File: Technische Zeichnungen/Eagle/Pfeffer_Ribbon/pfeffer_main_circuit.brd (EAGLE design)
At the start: 38 x 50 mm, 12 parts

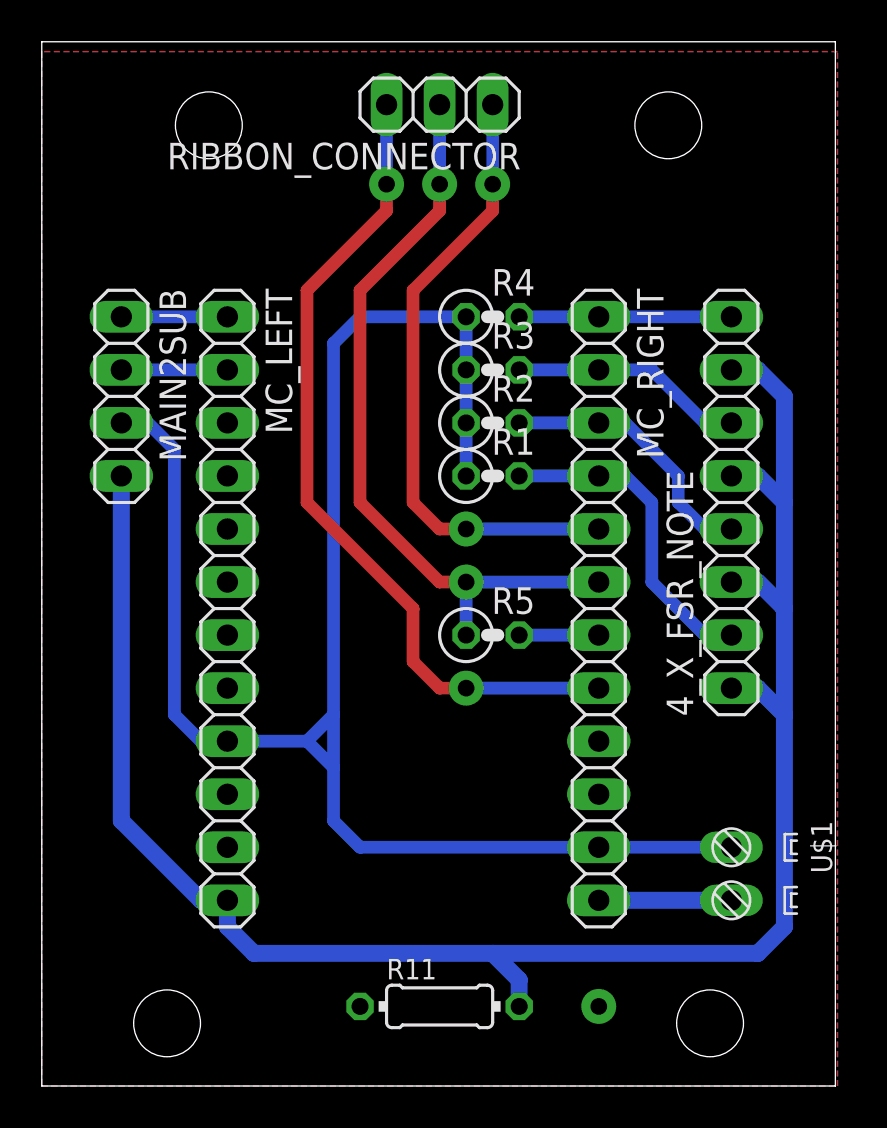
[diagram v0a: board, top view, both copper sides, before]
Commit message: added ribbon testing, firmware and applied it to the new firmware, added a new tech. drawing, added new PCB layouts
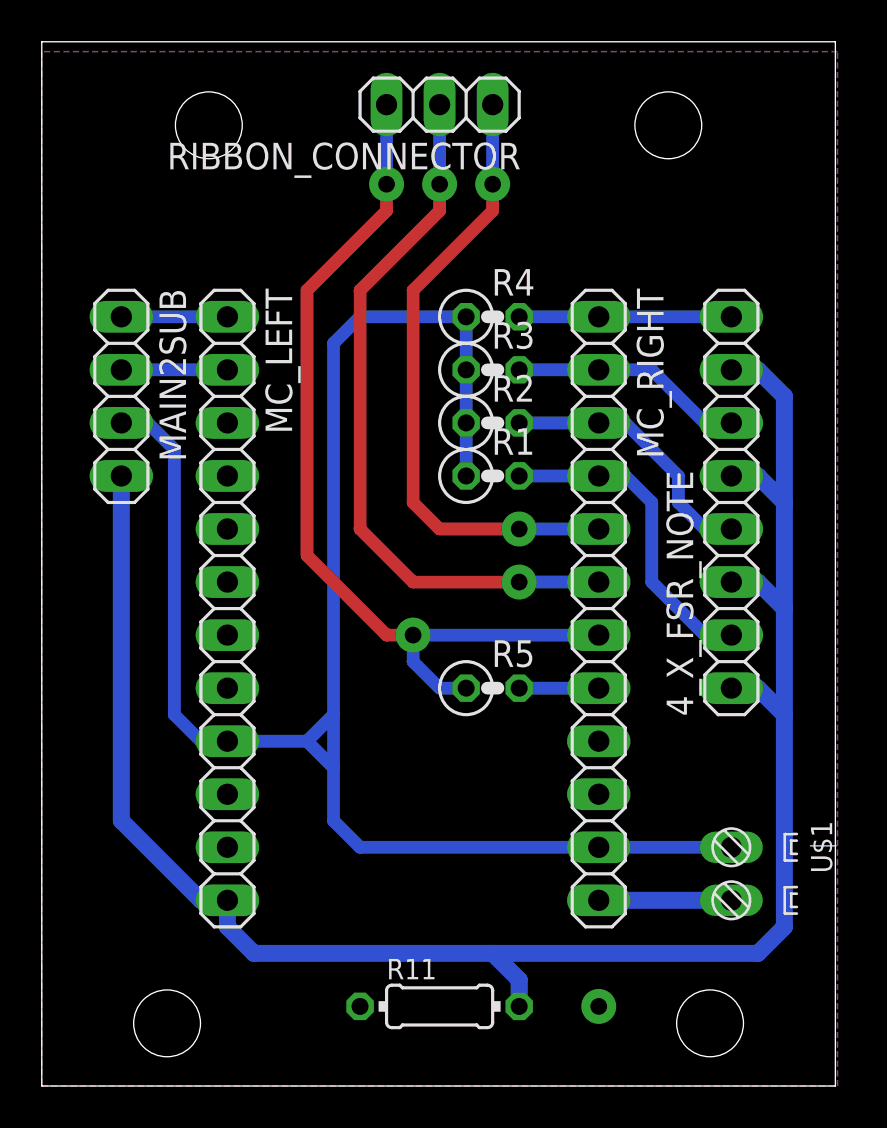
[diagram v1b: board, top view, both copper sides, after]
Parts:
- R11: value 100k -> 24
- moved R5 2.54 mm to (21.6, 19.1)
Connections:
- net N$10: now also MC_RIGHT.7, RIBBON_CONNECTOR.3; no longer MC_RIGHT.6, RIBBON_CONNECTOR.2
- net N$11: now also R5.2; no longer RIBBON_CONNECTOR.3
- net N$9: now also MC_RIGHT.6, RIBBON_CONNECTOR.2; no longer MC_RIGHT.7, R5.2
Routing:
- net N$11: track 39.8 -> 3.81 mm, vias 2 -> 0
- net N$9: track 3.81 -> 34.4 mm, vias 0 -> 2
- net N$10: track 36.2 -> 43.1 mm
- added copper zone on layer 16, net N$12
- added copper zone on layer 1, net N$13
- removed copper zone on layer 16, net GND
- removed copper zone on layer 1, net N$12
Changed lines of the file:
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@@
 <element name="R3" library="rcl" package="0207/2V" value="10k" x="21.59" y="34.29"/>
 <element name="R4" library="rcl" package="0207/2V" value="10k" x="21.59" y="36.83"/>
-<element name="R11" library="rcl" package="0204/7" value="100k" x="19.05" y="3.81"/>
+<element name="R11" library="rcl" package="0204/7" value="24" x="19.05" y="3.81"/>
 <element name="U$1" library="myDegsonConnectors" package="DS308-2.54-02P" value="DS308-02" x="33.02" y="10.16" rot="R270"/>
 <element name="RIBBON_CONNECTOR" library="pinhead" package="1X03" value="" x="19.05" y="46.99" rot="R180"/>
-<element name="R5" library="rcl" package="0207/2V" value="4.6k" x="21.59" y="21.59"/>
+<element name="R5" library="rcl" package="0207/2V" value="4.6k" x="21.59" y="19.05"/>
 </elements>
 <signals>
@@
 <wire x1="15.24" y1="11.43" x2="26.67" y2="11.43" width="0.6096" layer="16"/>
 <wire x1="13.97" y1="17.78" x2="13.97" y2="15.24" width="0.6096" layer="16"/>
-<polygon width="0.6096" layer="16">
-<vertex x="0" y="49.53"/>
-<vertex x="0" y="0"/>
-<vertex x="38.1" y="0"/>
-<vertex x="38.1" y="49.53"/>
-</polygon>
+<wire x1="26.67" y1="11.43" x2="26.67" y2="3.81" width="0" layer="19" extent="1-1"/>
+<wire x1="15.24" y1="3.81" x2="15.24" y2="11.43" width="0" layer="19" extent="16-16"/>
 </signal>
 <signal name="N$1">
@@
 <wire x1="3.81" y1="34.29" x2="8.89" y2="34.29" width="0.6096" layer="16"/>
 </signal>
+<signal name="N$5">
+<contactref element="MC_RIGHT" pad="12"/>
+<contactref element="U$1" pad="2"/>
+<wire x1="33.02" y1="8.89" x2="26.67" y2="8.89" width="0.8128" layer="16"/>
+</signal>
 <signal name="N$7">
+<contactref element="RIBBON_CONNECTOR" pad="1"/>
 <contactref element="MC_RIGHT" pad="5"/>
-<contactref element="RIBBON_CONNECTOR" pad="1"/>
-<via x="20.32" y="26.67" extent="1-16" drill="0.8" diameter="1.6764" shape="octagon"/>
+<wire x1="21.59" y1="46.99" x2="21.59" y2="43.18" width="0.6096" layer="16"/>
 <via x="21.59" y="43.18" extent="1-16" drill="0.8" diameter="1.6764" shape="octagon"/>
-<wire x1="21.59" y1="43.18" x2="21.59" y2="46.99" width="0.6096" layer="16"/>
-<wire x1="17.78" y1="38.1" x2="21.59" y2="41.91" width="0.6096" layer="1"/>
-<wire x1="21.59" y1="41.91" x2="21.59" y2="43.18" width="0.6096" layer="1"/>
-<wire x1="20.32" y1="26.67" x2="26.67" y2="26.67" width="0.6096" layer="16"/>
-<wire x1="20.32" y1="26.67" x2="19.05" y2="26.67" width="0.6096" layer="1"/>
-<wire x1="19.05" y1="26.67" x2="17.78" y2="27.94" width="0.6096" layer="1"/>
-<wire x1="17.78" y1="27.94" x2="17.78" y2="38.1" width="0.6096" layer="1"/>
+<wire x1="21.59" y1="43.18" x2="21.59" y2="41.91" width="0.6096" layer="1"/>
+<wire x1="21.59" y1="41.91" x2="17.78" y2="38.1" width="0.6096" layer="1"/>
+<via x="22.86" y="26.67" extent="1-16" drill="0.8" diameter="1.6764" shape="octagon"/>
+<wire x1="22.86" y1="26.67" x2="26.67" y2="26.67" width="0.6096" layer="16"/>
+<wire x1="17.78" y1="38.1" x2="17.78" y2="27.94" width="0.6096" layer="1"/>
+<wire x1="17.78" y1="27.94" x2="19.05" y2="26.67" width="0.6096" layer="1"/>
+<wire x1="19.05" y1="26.67" x2="22.86" y2="26.67" width="0.6096" layer="1"/>
 </signal>
-<signal name="N$10">
+<signal name="N$9">
 <contactref element="RIBBON_CONNECTOR" pad="2"/>
 <contactref element="MC_RIGHT" pad="6"/>
@@
 <via x="19.05" y="43.18" extent="1-16" drill="0.8" diameter="1.6764" shape="octagon"/>
 <wire x1="19.05" y1="43.18" x2="19.05" y2="41.91" width="0.6096" layer="1"/>
-<wire x1="15.24" y1="38.1" x2="19.05" y2="41.91" width="0.6096" layer="1"/>
-<via x="20.32" y="24.13" extent="1-16" drill="0.8" diameter="1.6764" shape="octagon"/>
-<wire x1="20.32" y1="24.13" x2="19.05" y2="24.13" width="0.6096" layer="1"/>
-<wire x1="19.05" y1="24.13" x2="15.24" y2="27.94" width="0.6096" layer="1"/>
-<wire x1="15.24" y1="27.94" x2="15.24" y2="38.1" width="0.6096" layer="1"/>
-<wire x1="26.67" y1="24.13" x2="20.32" y2="24.13" width="0.6096" layer="16"/>
+<wire x1="19.05" y1="41.91" x2="15.24" y2="38.1" width="0.6096" layer="1"/>
+<via x="22.86" y="24.13" extent="1-16" drill="0.8" diameter="1.6764" shape="octagon"/>
+<wire x1="22.86" y1="24.13" x2="26.67" y2="24.13" width="0.6096" layer="16"/>
+<wire x1="15.24" y1="38.1" x2="15.24" y2="26.67" width="0.6096" layer="1"/>
+<wire x1="15.24" y1="26.67" x2="17.78" y2="24.13" width="0.6096" layer="1"/>
+<wire x1="17.78" y1="24.13" x2="22.86" y2="24.13" width="0.6096" layer="1"/>
+</signal>
+<signal name="N$10">
+<contactref element="RIBBON_CONNECTOR" pad="3"/>
+<contactref element="MC_RIGHT" pad="7"/>
+<wire x1="16.51" y1="46.99" x2="16.51" y2="43.18" width="0.6096" layer="16"/>
+<via x="16.51" y="43.18" extent="1-16" drill="0.8" diameter="1.6764" shape="octagon"/>
+<wire x1="16.51" y1="43.18" x2="16.51" y2="41.91" width="0.6096" layer="1"/>
+<wire x1="16.51" y1="41.91" x2="12.7" y2="38.1" width="0.6096" layer="1"/>
+<via x="17.78" y="21.59" extent="1-16" drill="0.8" diameter="1.6764" shape="octagon"/>
+<wire x1="26.67" y1="21.59" x2="17.78" y2="21.59" width="0.6096" layer="16"/>
+<wire x1="12.7" y1="38.1" x2="12.7" y2="25.4" width="0.6096" layer="1"/>
+<wire x1="16.51" y1="21.59" x2="17.78" y2="21.59" width="0.6096" layer="1"/>
+<wire x1="12.7" y1="25.4" x2="16.51" y2="21.59" width="0.6096" layer="1"/>
 <contactref element="R5" pad="1"/>
-<wire x1="20.32" y1="24.13" x2="20.32" y2="21.59" width="0.6096" layer="16"/>
+<wire x1="17.78" y1="21.59" x2="17.78" y2="20.32" width="0.6096" layer="16"/>
+<wire x1="17.78" y1="20.32" x2="19.05" y2="19.05" width="0.6096" layer="16"/>
+<wire x1="19.05" y1="19.05" x2="20.32" y2="19.05" width="0.6096" layer="16"/>
 </signal>
 <signal name="N$11">
+<contactref element="R5" pad="2"/>
 <contactref element="MC_RIGHT" pad="8"/>
-<contactref element="RIBBON_CONNECTOR" pad="3"/>
-<wire x1="16.51" y1="46.99" x2="16.51" y2="43.18" width="0.6096" layer="16"/>
-<via x="16.51" y="43.18" extent="1-16" drill="0.8" diameter="1.6764" shape="octagon"/>
-<wire x1="12.7" y1="38.1" x2="16.51" y2="41.91" width="0.6096" layer="1"/>
-<via x="20.32" y="19.05" extent="1-16" drill="0.8" diameter="1.6764" shape="octagon"/>
-<wire x1="16.51" y1="43.18" x2="16.51" y2="41.91" width="0.6096" layer="1"/>
-<wire x1="20.32" y1="19.05" x2="26.67" y2="19.05" width="0.6096" layer="16"/>
-<wire x1="12.7" y1="27.94" x2="17.78" y2="22.86" width="0.6096" layer="1"/>
-<wire x1="12.7" y1="27.94" x2="12.7" y2="38.1" width="0.6096" layer="1"/>
-<wire x1="17.78" y1="22.86" x2="17.78" y2="20.32" width="0.6096" layer="1"/>
-<wire x1="17.78" y1="20.32" x2="19.05" y2="19.05" width="0.6096" layer="1"/>
-<wire x1="19.05" y1="19.05" x2="20.32" y2="19.05" width="0.6096" layer="1"/>
-</signal>
-<signal name="N$5">
-<contactref element="MC_RIGHT" pad="12"/>
-<contactref element="U$1" pad="2"/>
-<wire x1="33.02" y1="8.89" x2="26.67" y2="8.89" width="0.8128" layer="16"/>
-</signal>
-<signal name="N$9">
-<contactref element="MC_RIGHT" pad="7"/>
-<contactref element="R5" pad="2"/>
-<wire x1="22.86" y1="21.59" x2="26.67" y2="21.59" width="0.6096" layer="16"/>
+<wire x1="22.86" y1="19.05" x2="26.67" y2="19.05" width="0.6096" layer="16"/>
 </signal>
 <signal name="N$12">
-<polygon width="0.4064" layer="1">
+<polygon width="0.6096" layer="16">
 <vertex x="0" y="49.53"/>
 <vertex x="0" y="0"/>
+<vertex x="38.1" y="0"/>
+<vertex x="38.1" y="49.53"/>
+</polygon>
+</signal>
+<signal name="N$13">
+<polygon width="0.6096" layer="1">
+<vertex x="0" y="49.53"/>
+<vertex x="0" y="0"/>

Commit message: little but significant changes to  the schemtaics and circuit
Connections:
- new net N$14: MC_RIGHT.11, U$1.1
- net GND: no longer MC_RIGHT.11, U$1.1
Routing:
- net GND: track 83.2 -> 56.7 mm
- net N$14: track 0.00 -> 6.35 mm
- added copper zone on layer 16, net GND
- added copper zone on layer 1, net N$12
- removed copper zone on layer 16, net N$12
- removed copper zone on layer 1, net N$13
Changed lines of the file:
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@@
 <contactref element="R3" pad="1"/>
 <contactref element="R4" pad="1"/>
-<contactref element="MC_RIGHT" pad="11"/>
 <contactref element="MAIN2SUB" pad="3"/>
 <wire x1="20.32" y1="36.83" x2="20.32" y2="34.29" width="0.6096" layer="16"/>
@@
 <wire x1="7.62" y1="16.51" x2="8.89" y2="16.51" width="0.6096" layer="16"/>
 <contactref element="R11" pad="1"/>
-<contactref element="U$1" pad="1"/>
-<wire x1="26.67" y1="11.43" x2="33.02" y2="11.43" width="0.6096" layer="16"/>
 <wire x1="8.89" y1="16.51" x2="12.7" y2="16.51" width="0.6096" layer="16"/>
 <wire x1="12.7" y1="16.51" x2="13.97" y2="17.78" width="0.6096" layer="16"/>
@@
 <wire x1="13.97" y1="35.56" x2="15.24" y2="36.83" width="0.6096" layer="16"/>
 <wire x1="15.24" y1="36.83" x2="20.32" y2="36.83" width="0.6096" layer="16"/>
-<wire x1="13.97" y1="15.24" x2="12.7" y2="16.51" width="0.6096" layer="16"/>
-<wire x1="13.97" y1="15.24" x2="13.97" y2="12.7" width="0.6096" layer="16"/>
-<wire x1="13.97" y1="12.7" x2="15.24" y2="11.43" width="0.6096" layer="16"/>
-<wire x1="15.24" y1="11.43" x2="26.67" y2="11.43" width="0.6096" layer="16"/>
-<wire x1="13.97" y1="17.78" x2="13.97" y2="15.24" width="0.6096" layer="16"/>
-<wire x1="26.67" y1="11.43" x2="26.67" y2="3.81" width="0" layer="19" extent="1-1"/>
-<wire x1="15.24" y1="3.81" x2="15.24" y2="11.43" width="0" layer="19" extent="16-16"/>
+<polygon width="0.4064" layer="16">
+<vertex x="0" y="49.53"/>
+<vertex x="0" y="0"/>
+<vertex x="38.1" y="0"/>
+<vertex x="38.1" y="49.53"/>
+</polygon>
 </signal>
 <signal name="N$1">
@@
 <wire x1="22.86" y1="19.05" x2="26.67" y2="19.05" width="0.6096" layer="16"/>
 </signal>
+<signal name="N$14">
+<contactref element="MC_RIGHT" pad="11"/>
+<contactref element="U$1" pad="1"/>
+<wire x1="33.02" y1="11.43" x2="26.67" y2="11.43" width="0.6096" layer="16"/>
+</signal>
 <signal name="N$12">
-<polygon width="0.6096" layer="16">
+<polygon width="0.4064" layer="1">
 <vertex x="0" y="49.53"/>
 <vertex x="0" y="0"/>
-<vertex x="38.1" y="0"/>
-<vertex x="38.1" y="49.53"/>
-</polygon>
-</signal>
-<signal name="N$13">
-<polygon width="0.6096" layer="1">
-<vertex x="0" y="49.53"/>
-<vertex x="0" y="0"/>
